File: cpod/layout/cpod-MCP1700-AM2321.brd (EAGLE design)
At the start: 16 parts, among them IC1 PCF8563DIP, Y1 32.768kHz

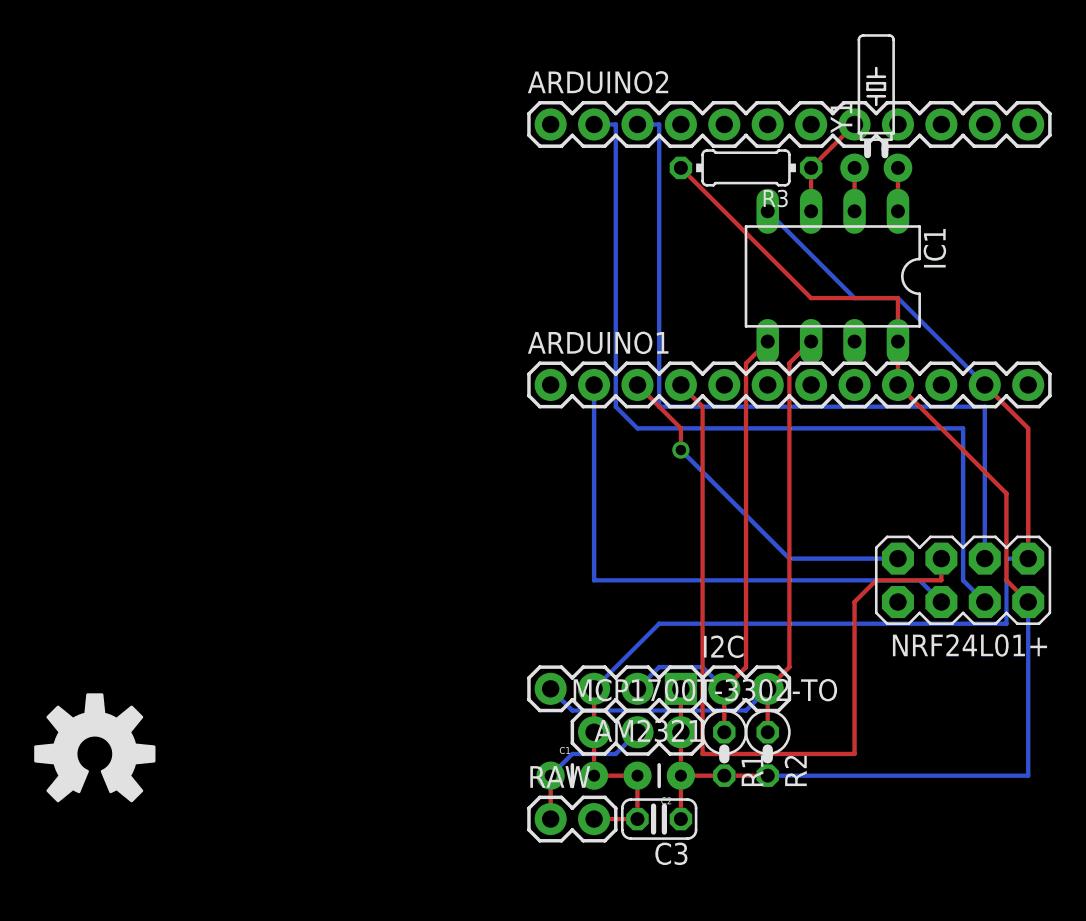
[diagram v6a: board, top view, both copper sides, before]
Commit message: 调整了PCB，变得更清晰一些
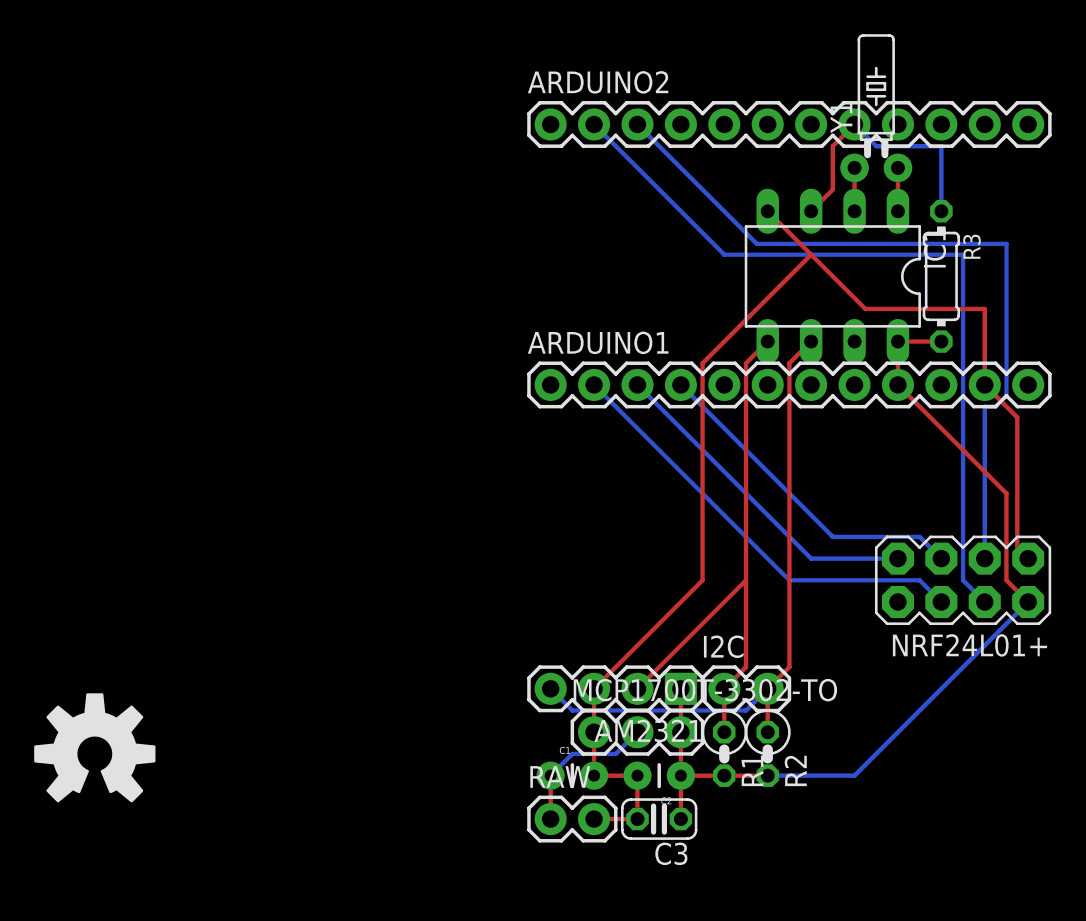
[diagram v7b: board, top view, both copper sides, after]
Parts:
- moved R3 13.1 mm to (54.6, -10.2), turned to 270 degrees
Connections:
- removed net IRQ: NRF24L01+.8
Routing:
- net SCK: track 46.8 -> 19.4 mm
- net VCC: track 74.9 -> 53.1 mm
- net INT0: track 6.13 -> 15.5 mm
- net MOSI: track 32.3 -> 25.6 mm
- net CSN: track 49.3 -> 45.6 mm
- net SDA: track 30.0 -> 32.9 mm
- net GND: track 71.6 -> 74.1 mm
- net CE: track 45.7 -> 43.8 mm
- net MISO: track 20.2 -> 19.4 mm, vias 1 -> 0
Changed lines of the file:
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@@
 <autorouter>
 <pass name="Default">
-<param name="RoutingGrid" value="50mil"/>
+<param name="RoutingGrid" value="25mil"/>
 <param name="tpViaShape" value="round"/>
 <param name="PrefDir.1" value="|"/>
@@
 <element name="Y1" library="SparkFun-FreqCtrl" package="TC26H" value="32.768kHz" x="50.8" y="-3.81"/>
 <element name="C3" library="rcl" package="C025-024X044" value="100nF" x="38.1" y="-41.91" rot="R180"/>
-<element name="R3" library="rcl" package="0204/7" value="5.1k" x="43.18" y="-3.81" rot="R180"/>
+<element name="R3" library="rcl" package="0204/7" value="5.1k" x="54.61" y="-10.16" rot="R270"/>
 </elements>
 <signals>
@@
 <wire x1="34.29" y1="-36.83" x2="34.29" y2="-34.29" width="0.254" layer="1"/>
 <wire x1="36.83" y1="-39.37" x2="36.83" y2="-41.91" width="0.254" layer="1"/>
-<wire x1="49.53" y1="-11.43" x2="44.45" y2="-6.35" width="0.254" layer="16"/>
-<wire x1="52.07" y1="-11.43" x2="49.53" y2="-11.43" width="0.254" layer="16"/>
-<wire x1="57.15" y1="-16.51" x2="52.07" y2="-11.43" width="0.254" layer="16"/>
-<wire x1="59.69" y1="-19.05" x2="59.69" y2="-26.67" width="0.254" layer="1"/>
-<wire x1="57.15" y1="-16.51" x2="59.69" y2="-19.05" width="0.254" layer="1"/>
-<wire x1="38.1" y1="-30.48" x2="34.29" y2="-34.29" width="0.254" layer="16"/>
-<wire x1="58.42" y1="-30.48" x2="38.1" y2="-30.48" width="0.254" layer="16"/>
-<wire x1="58.42" y1="-26.67" x2="58.42" y2="-30.48" width="0.254" layer="16"/>
-<wire x1="59.69" y1="-26.67" x2="58.42" y2="-26.67" width="0.254" layer="16"/>
+<wire x1="50.165" y1="-12.065" x2="46.99" y2="-8.89" width="0.254" layer="1"/>
+<wire x1="46.99" y1="-8.89" x2="44.45" y2="-6.35" width="0.254" layer="1"/>
+<wire x1="57.15" y1="-12.065" x2="50.165" y2="-12.065" width="0.254" layer="1"/>
+<wire x1="57.15" y1="-16.51" x2="57.15" y2="-12.065" width="0.254" layer="1"/>
+<wire x1="59.055" y1="-26.035" x2="59.69" y2="-26.67" width="0.254" layer="1"/>
+<wire x1="59.055" y1="-18.415" x2="59.055" y2="-26.035" width="0.254" layer="1"/>
+<wire x1="57.15" y1="-16.51" x2="59.055" y2="-18.415" width="0.254" layer="1"/>
+<wire x1="40.64" y1="-27.94" x2="34.29" y2="-34.29" width="0.254" layer="1"/>
+<wire x1="40.64" y1="-15.24" x2="40.64" y2="-27.94" width="0.254" layer="1"/>
+<wire x1="46.99" y1="-8.89" x2="40.64" y2="-15.24" width="0.254" layer="1"/>
 </signal>
 <signal name="SDA">
@@
 <wire x1="41.91" y1="-34.29" x2="41.91" y2="-36.83" width="0.254" layer="1"/>
 <wire x1="43.18" y1="-15.24" x2="44.45" y2="-13.97" width="0.254" layer="1"/>
-<wire x1="43.18" y1="-33.02" x2="43.18" y2="-15.24" width="0.254" layer="1"/>
+<wire x1="43.18" y1="-33.02" x2="43.18" y2="-27.94" width="0.254" layer="1"/>
+<wire x1="43.18" y1="-27.94" x2="43.18" y2="-15.24" width="0.254" layer="1"/>
 <wire x1="41.91" y1="-34.29" x2="43.18" y2="-33.02" width="0.254" layer="1"/>
-<wire x1="38.1" y1="-33.02" x2="36.83" y2="-34.29" width="0.254" layer="16"/>
-<wire x1="40.64" y1="-33.02" x2="38.1" y2="-33.02" width="0.254" layer="16"/>
-<wire x1="41.91" y1="-34.29" x2="40.64" y2="-33.02" width="0.254" layer="16"/>
+<wire x1="43.18" y1="-27.94" x2="36.83" y2="-34.29" width="0.254" layer="1"/>
 </signal>
 <signal name="VCC">
@@
 <contactref element="C3" pad="1"/>
 <contactref element="R3" pad="2"/>
-<wire x1="46.99" y1="-11.43" x2="39.37" y2="-3.81" width="0.254" layer="1"/>
-<wire x1="52.07" y1="-11.43" x2="46.99" y2="-11.43" width="0.254" layer="1"/>
-<wire x1="52.07" y1="-13.97" x2="52.07" y2="-11.43" width="0.254" layer="1"/>
-<wire x1="52.07" y1="-13.97" x2="52.07" y2="-16.51" width="0.254" layer="1"/>
+<wire x1="54.61" y1="-13.97" x2="52.07" y2="-13.97" width="0.254" layer="1"/>
+<wire x1="52.07" y1="-16.51" x2="52.07" y2="-13.97" width="0.254" layer="1"/>
 <wire x1="39.37" y1="-34.29" x2="39.37" y2="-36.83" width="0.254" layer="1"/>
 <wire x1="39.37" y1="-39.37" x2="39.37" y2="-41.91" width="0.254" layer="1"/>
 <wire x1="39.37" y1="-39.37" x2="41.91" y2="-39.37" width="0.254" layer="1"/>
 <wire x1="41.91" y1="-39.37" x2="44.45" y2="-39.37" width="0.254" layer="1"/>
-<wire x1="59.69" y1="-39.37" x2="59.69" y2="-29.21" width="0.254" layer="16"/>
-<wire x1="44.45" y1="-39.37" x2="59.69" y2="-39.37" width="0.254" layer="16"/>
+<wire x1="49.53" y1="-39.37" x2="59.69" y2="-29.21" width="0.254" layer="16"/>
+<wire x1="44.45" y1="-39.37" x2="49.53" y2="-39.37" width="0.254" layer="16"/>
 <wire x1="39.37" y1="-39.37" x2="39.37" y2="-36.83" width="0.254" layer="1"/>
 <wire x1="58.42" y1="-22.86" x2="52.07" y2="-16.51" width="0.254" layer="1"/>
@@
 <contactref element="ARDUINO1" pad="4"/>
 <contactref element="NRF24L01+" pad="5"/>
-<wire x1="40.64" y1="-17.78" x2="39.37" y2="-16.51" width="0.254" layer="1"/>
-<wire x1="40.64" y1="-38.1" x2="40.64" y2="-17.78" width="0.254" layer="1"/>
-<wire x1="49.53" y1="-38.1" x2="40.64" y2="-38.1" width="0.254" layer="1"/>
-<wire x1="49.53" y1="-29.21" x2="49.53" y2="-38.1" width="0.254" layer="1"/>
-<wire x1="50.8" y1="-27.94" x2="49.53" y2="-29.21" width="0.254" layer="1"/>
-<wire x1="54.61" y1="-27.94" x2="50.8" y2="-27.94" width="0.254" layer="1"/>
-<wire x1="54.61" y1="-26.67" x2="54.61" y2="-27.94" width="0.254" layer="1"/>
+<wire x1="48.26" y1="-25.4" x2="39.37" y2="-16.51" width="0.254" layer="16"/>
+<wire x1="53.34" y1="-25.4" x2="48.26" y2="-25.4" width="0.254" layer="16"/>
+<wire x1="54.61" y1="-26.67" x2="53.34" y2="-25.4" width="0.254" layer="16"/>
 </signal>
 <signal name="MISO">
 <contactref element="ARDUINO1" pad="3"/>
 <contactref element="NRF24L01+" pad="7"/>
-<wire x1="39.37" y1="-19.05" x2="36.83" y2="-16.51" width="0.254" layer="1"/>
-<wire x1="39.37" y1="-20.32" x2="39.37" y2="-19.05" width="0.254" layer="1"/>
-<wire x1="45.72" y1="-26.67" x2="39.37" y2="-20.32" width="0.254" layer="16"/>
-<wire x1="52.07" y1="-26.67" x2="45.72" y2="-26.67" width="0.254" layer="16"/>
-<via x="39.37" y="-20.32" extent="1-16" drill="0.6096"/>
+<wire x1="46.99" y1="-26.67" x2="36.83" y2="-16.51" width="0.254" layer="16"/>
+<wire x1="52.07" y1="-26.67" x2="46.99" y2="-26.67" width="0.254" layer="16"/>
 </signal>
 <signal name="MOSI">
 <contactref element="ARDUINO1" pad="2"/>
 <contactref element="NRF24L01+" pad="6"/>
-<wire x1="34.29" y1="-27.94" x2="34.29" y2="-16.51" width="0.254" layer="16"/>
-<wire x1="53.34" y1="-27.94" x2="34.29" y2="-27.94" width="0.254" layer="16"/>
+<wire x1="45.72" y1="-27.94" x2="34.29" y2="-16.51" width="0.254" layer="16"/>
+<wire x1="53.34" y1="-27.94" x2="45.72" y2="-27.94" width="0.254" layer="16"/>
 <wire x1="54.61" y1="-29.21" x2="53.34" y2="-27.94" width="0.254" layer="16"/>
 </signal>
@@
 <contactref element="ARDUINO2" pad="2"/>
 <wire x1="55.88" y1="-27.94" x2="57.15" y2="-29.21" width="0.254" layer="16"/>
-<wire x1="55.88" y1="-19.05" x2="55.88" y2="-27.94" width="0.254" layer="16"/>
-<wire x1="36.83" y1="-19.05" x2="55.88" y2="-19.05" width="0.254" layer="16"/>
-<wire x1="35.56" y1="-17.78" x2="36.83" y2="-19.05" width="0.254" layer="16"/>
-<wire x1="35.56" y1="-1.27" x2="35.56" y2="-17.78" width="0.254" layer="16"/>
-<wire x1="34.29" y1="-1.27" x2="35.56" y2="-1.27" width="0.254" layer="16"/>
+<wire x1="55.88" y1="-8.89" x2="55.88" y2="-27.94" width="0.254" layer="16"/>
+<wire x1="41.91" y1="-8.89" x2="55.88" y2="-8.89" width="0.254" layer="16"/>
+<wire x1="34.29" y1="-1.27" x2="41.91" y2="-8.89" width="0.254" layer="16"/>
 </signal>
 <signal name="CE">
@@
 <contactref element="ARDUINO2" pad="3"/>
 <wire x1="57.15" y1="-17.78" x2="57.15" y2="-26.67" width="0.254" layer="16"/>
-<wire x1="38.1" y1="-17.78" x2="57.15" y2="-17.78" width="0.254" layer="16"/>
-<wire x1="38.1" y1="-1.27" x2="38.1" y2="-17.78" width="0.254" layer="16"/>
-<wire x1="36.83" y1="-1.27" x2="38.1" y2="-1.27" width="0.254" layer="16"/>
+<wire x1="57.785" y1="-17.78" x2="57.15" y2="-17.78" width="0.254" layer="16"/>
+<wire x1="58.42" y1="-17.145" x2="57.785" y2="-17.78" width="0.254" layer="16"/>
+<wire x1="58.42" y1="-8.255" x2="58.42" y2="-17.145" width="0.254" layer="16"/>
+<wire x1="43.815" y1="-8.255" x2="58.42" y2="-8.255" width="0.254" layer="16"/>
+<wire x1="36.83" y1="-1.27" x2="43.815" y2="-8.255" width="0.254" layer="16"/>
 </signal>
 <signal name="D9">
 <contactref element="ARDUINO2" pad="1"/>
-</signal>
-<signal name="IRQ">
-<contactref element="NRF24L01+" pad="8"/>
 </signal>
 <signal name="N$4">
@@
 <contactref element="ARDUINO2" pad="8"/>
 <contactref element="R3" pad="1"/>
-<wire x1="46.99" y1="-3.81" x2="46.99" y2="-6.35" width="0.254" layer="1"/>
-<wire x1="49.53" y1="-1.27" x2="46.99" y2="-3.81" width="0.254" layer="1"/>
+<wire x1="48.26" y1="-5.08" x2="46.99" y2="-6.35" width="0.254" layer="1"/>
+<wire x1="48.26" y1="-2.54" x2="48.26" y2="-5.08" width="0.254" layer="1"/>
+<wire x1="49.53" y1="-1.27" x2="48.26" y2="-2.54" width="0.254" layer="1"/>
+<wire x1="54.61" y1="-2.54" x2="54.61" y2="-6.35" width="0.254" layer="16"/>
+<wire x1="50.8" y1="-2.54" x2="54.61" y2="-2.54" width="0.254" layer="16"/>
+<wire x1="49.53" y1="-1.27" x2="50.8" y2="-2.54" width="0.254" layer="16"/>
 </signal>
 </signals>
